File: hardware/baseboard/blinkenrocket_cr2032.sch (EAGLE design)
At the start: 22 parts, among them SW1 SWITCH-4POMRON-6-6-SWITCH, SW2 SWITCH-4POMRON-6-6-SWITCH, U2 EEPROM-I2CEIAJ

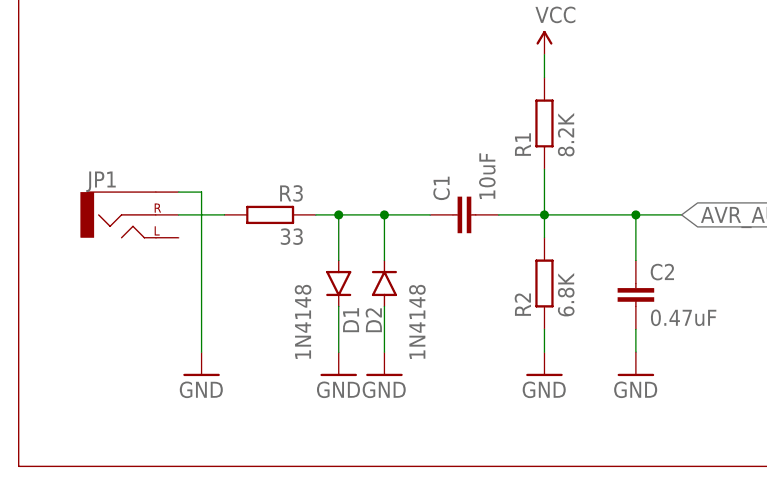
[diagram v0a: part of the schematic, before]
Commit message: 1206 instead of 0805 - this is easier to solder actually...
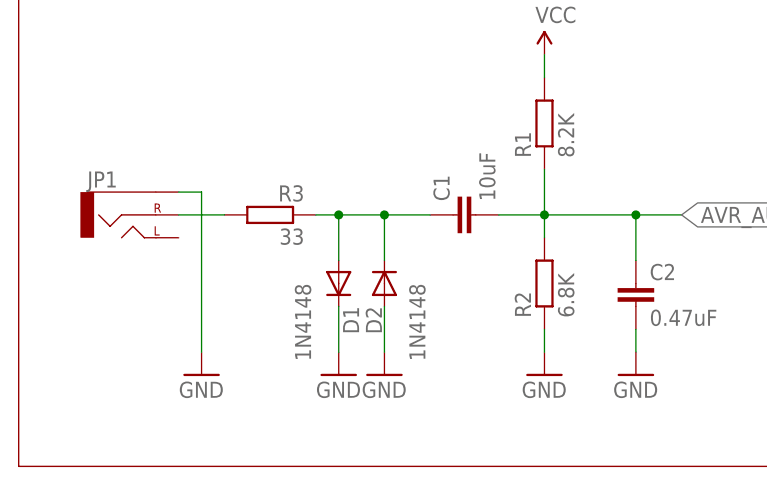
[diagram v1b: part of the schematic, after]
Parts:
- C1, C2, C3: device resistor:C-EUC0805K -> resistor:C-EUC1206
- D1, D2: device SparkFun-DiscreteSemi:DIODESOD -> diode-1:DIODE-SOD123
- R1, R2, R3, R4, R5, R6: device resistor:R-EU_M0805 -> resistor:R-EU_R1206
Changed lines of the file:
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@@
 <parts>
 <part name="JP1" library="SparkFun-Connectors" deviceset="AUDIO-JACK" device="PTH"/>
-<part name="C1" library="resistor" deviceset="C-EU" device="C0805K" value="10uF"/>
-<part name="C2" library="resistor" deviceset="C-EU" device="C0805K" value="0.47uF"/>
-<part name="R1" library="resistor" deviceset="R-EU_" device="M0805" value="8.2K"/>
-<part name="R2" library="resistor" deviceset="R-EU_" device="M0805" value="6.8K"/>
-<part name="R3" library="resistor" deviceset="R-EU_" device="M0805" value="33"/>
-<part name="D2" library="SparkFun-DiscreteSemi" deviceset="DIODE" device="SOD" value="1N4148"/>
-<part name="D1" library="SparkFun-DiscreteSemi" deviceset="DIODE" device="SOD" value="1N4148"/>
+<part name="C1" library="resistor" deviceset="C-EU" device="C1206" value="10uF"/>
+<part name="C2" library="resistor" deviceset="C-EU" device="C1206" value="0.47uF"/>
+<part name="R1" library="resistor" deviceset="R-EU_" device="R1206" value="8.2K"/>
+<part name="R2" library="resistor" deviceset="R-EU_" device="R1206" value="6.8K"/>
+<part name="R3" library="resistor" deviceset="R-EU_" device="R1206" value="33"/>
+<part name="D2" library="diode-1" deviceset="DIODE-" device="SOD123" value="1N4148"/>
+<part name="D1" library="diode-1" deviceset="DIODE-" device="SOD123" value="1N4148"/>
 <part name="GND3" library="SparkFun-Aesthetics" deviceset="GND" device=""/>
 <part name="SUPPLY1" library="SparkFun-Aesthetics" deviceset="VCC" device=""/>
@@
 <part name="GND11" library="SparkFun-Aesthetics" deviceset="GND" device=""/>
 <part name="GND12" library="SparkFun-Aesthetics" deviceset="GND" device=""/>
-<part name="C3" library="resistor" deviceset="C-EU" device="C0805K" value="0.47uF"/>
+<part name="C3" library="resistor" deviceset="C-EU" device="C1206" value="0.47uF"/>
 <part name="U$1" library="kzh20_lithium_batterie_holder" deviceset="2032" device=""/>
 <part name="SW1" library="switch" deviceset="SWITCH-4P" device="OMRON-6-6-SWITCH"/>
@@
 <part name="U$2" library="avr-muzy" deviceset="TINY48/88" device="B" value="ATTINY88"/>
 <part name="U2" library="SparkFun-DigitalIC" deviceset="EEPROM-I2C" device="EIAJ"/>
-<part name="R4" library="resistor" deviceset="R-EU_" device="M0805" value="10K"/>
-<part name="R5" library="resistor" deviceset="R-EU_" device="M0805" value="10K"/>
+<part name="R4" library="resistor" deviceset="R-EU_" device="R1206" value="10K"/>
+<part name="R5" library="resistor" deviceset="R-EU_" device="R1206" value="10K"/>
 <part name="GND1" library="SparkFun-Aesthetics" deviceset="GND" device=""/>
 <part name="GND2" library="SparkFun-Aesthetics" deviceset="GND" device=""/>
@@
 <part name="JP3" library="pinhead-2" deviceset="PINHD-1X05" device="_2.54-S"/>
 <part name="JP4" library="pinhead-2" deviceset="PINHD-1X05" device="_2.54-S"/>
-<part name="R6" library="resistor" deviceset="R-EU_" device="M0805" value="10K"/>
+<part name="R6" library="resistor" deviceset="R-EU_" device="R1206" value="10K"/>
 <part name="SUPPLY2" library="SparkFun-Aesthetics" deviceset="VCC" device=""/>
 <part name="U$3" library="computronics.com.au" deviceset="BATTERYPAD" device=""/>
